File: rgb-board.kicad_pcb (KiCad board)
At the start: 2 copper layers, 178 x 129.5 mm, 91 parts, among them J1 Conn_02x25_Odd_Even, J10 RCJ-2223, J3 TEST_1P, J4 TEST_1P, J5 73415-3980, J6 73415-3980, J7 73415-3980, J8 73415-3980, J9 73415-3980, Q101 BC850C, Q105 BC850C, Q109 BC850C, Q113 BC850C, Q114 BC850C, Q201 BC850C, SW101 JS202011SCQN, SW105 JS202011SCQN, SW129 JS202011SCQN, SW143 JS202011SCQN, SW152 JS202011SCQN, U1 NCP1117-12_SOT223

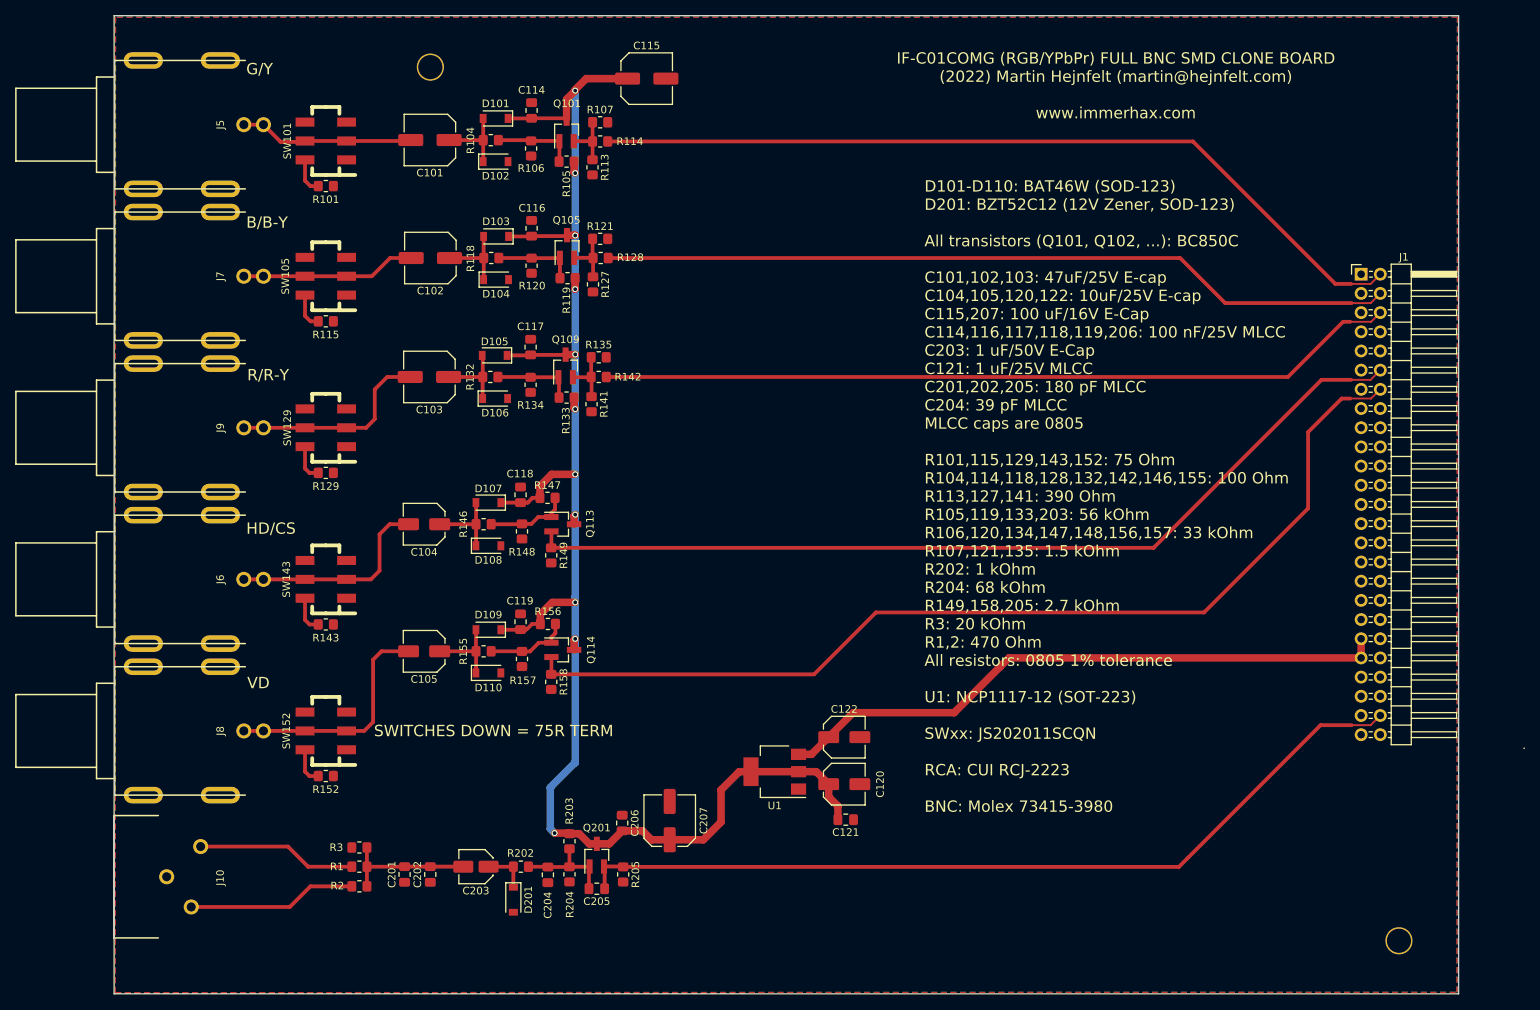
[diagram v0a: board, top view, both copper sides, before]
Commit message: Add optional segments, update to Kicad 6
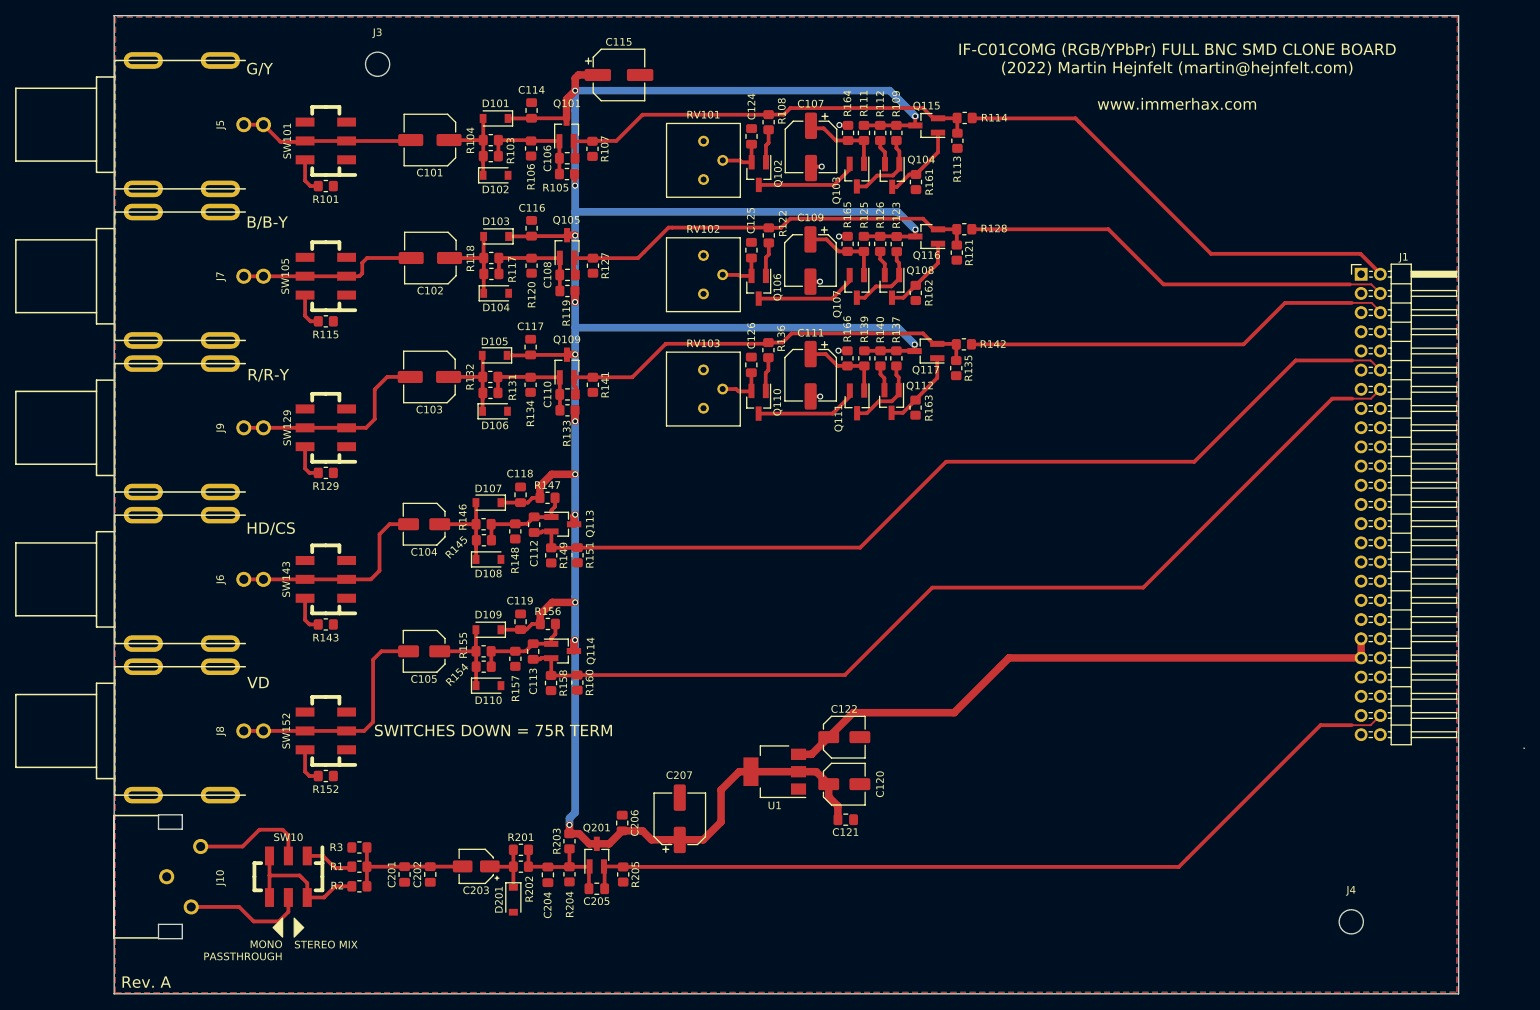
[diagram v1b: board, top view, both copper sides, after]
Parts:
- added C106: OPT, Capacitor_SMD:C_0805_2012Metric_Pad1.18x1.45mm_HandSolder, F.Cu at (109.8, 49.3)
- added C107: 100uF/16, Capacitor_SMD:CP_Elec_6.3x5.4, F.Cu at (142.1, 47.8)
- added C108: OPT, Capacitor_SMD:C_0805_2012Metric_Pad1.18x1.45mm_HandSolder, F.Cu at (109.9, 64.7)
- added C109: 100uF/16, Capacitor_SMD:CP_Elec_6.3x5.4, F.Cu at (142.0, 62.8)
- added C110: OPT, Capacitor_SMD:C_0805_2012Metric_Pad1.18x1.45mm_HandSolder, F.Cu at (109.9, 80.5)
- added C111: 100uF/16, Capacitor_SMD:CP_Elec_6.3x5.4, F.Cu at (142.0, 78.0)
- added C112: OPT, Capacitor_SMD:C_0805_2012Metric_Pad1.18x1.45mm_HandSolder, F.Cu at (105.4, 97.8)
- added C113: OPT, Capacitor_SMD:C_0805_2012Metric_Pad1.18x1.45mm_HandSolder, F.Cu at (105.3, 114.6)
- added C124: 15pF, Capacitor_SMD:C_0805_2012Metric_Pad1.18x1.45mm_HandSolder, F.Cu at (134.2, 46.4)
- added C125: 15pF, Capacitor_SMD:C_0805_2012Metric_Pad1.18x1.45mm_HandSolder, F.Cu at (134.2, 61.4)
- added C126: 15pF, Capacitor_SMD:C_0805_2012Metric_Pad1.18x1.45mm_HandSolder, F.Cu at (134.2, 76.6)
- added Q102: BC850C, Package_TO_SOT_SMD:SOT-23_Handsoldering, F.Cu at (135.2, 51.3)
- added Q103: BC850C, Package_TO_SOT_SMD:SOT-23_Handsoldering, F.Cu at (148.2, 51.5)
- added Q104: BC860C, Package_TO_SOT_SMD:SOT-23_Handsoldering, F.Cu at (152.8, 51.6)
- added Q106: BC850C, Package_TO_SOT_SMD:SOT-23_Handsoldering, F.Cu at (135.2, 66.4)
- added Q107: BC850C, Package_TO_SOT_SMD:SOT-23_Handsoldering, F.Cu at (148.2, 66.2)
- added Q108: BC860C, Package_TO_SOT_SMD:SOT-23_Handsoldering, F.Cu at (152.8, 66.2)
- added Q110: BC850C, Package_TO_SOT_SMD:SOT-23_Handsoldering, F.Cu at (135.2, 81.6)
- added Q111: BC850C, Package_TO_SOT_SMD:SOT-23_Handsoldering, F.Cu at (148.2, 81.5)
- added Q112: BC860C, Package_TO_SOT_SMD:SOT-23_Handsoldering, F.Cu at (152.8, 81.5)
- added Q115: OPT, Package_TO_SOT_SMD:SOT-23_Handsoldering, F.Cu at (157.4, 44.9)
- added Q116: OPT, Package_TO_SOT_SMD:SOT-23_Handsoldering, F.Cu at (157.4, 59.6)
- added Q117: OPT, Package_TO_SOT_SMD:SOT-23_Handsoldering, F.Cu at (157.3, 74.8)
- added R103: OPT, Resistor_SMD:R_0805_2012Metric_Pad1.20x1.40mm_HandSolder, F.Cu at (99.7, 49.0)
- added R108: OPT, Resistor_SMD:R_0805_2012Metric_Pad1.20x1.40mm_HandSolder, F.Cu at (136.5, 44.5)
- added R109: 470R, Resistor_SMD:R_0805_2012Metric_Pad1.20x1.40mm_HandSolder, F.Cu at (153.4, 45.9)
- added R111: 47k, Resistor_SMD:R_0805_2012Metric_Pad1.20x1.40mm_HandSolder, F.Cu at (149.1, 45.9)
- added R112: 470R, Resistor_SMD:R_0805_2012Metric_Pad1.20x1.40mm_HandSolder, F.Cu at (151.3, 45.9)
- added R117: 100, Resistor_SMD:R_0805_2012Metric_Pad1.20x1.40mm_HandSolder, F.Cu at (99.8, 64.6)
- added R122: OPT, Resistor_SMD:R_0805_2012Metric_Pad1.20x1.40mm_HandSolder, F.Cu at (136.5, 59.5)
- added R123: 470R, Resistor_SMD:R_0805_2012Metric_Pad1.20x1.40mm_HandSolder, F.Cu at (153.4, 60.6)
- added R125: 47k, Resistor_SMD:R_0805_2012Metric_Pad1.20x1.40mm_HandSolder, F.Cu at (149.1, 60.6)
- added R126: 470R, Resistor_SMD:R_0805_2012Metric_Pad1.20x1.40mm_HandSolder, F.Cu at (151.2, 60.6)
- added R131: OPT, Resistor_SMD:R_0805_2012Metric_Pad1.20x1.40mm_HandSolder, F.Cu at (99.6, 80.3)
- added R136: OPT, Resistor_SMD:R_0805_2012Metric_Pad1.20x1.40mm_HandSolder, F.Cu at (136.4, 74.7)
- added R137: 470R, Resistor_SMD:R_0805_2012Metric_Pad1.20x1.40mm_HandSolder, F.Cu at (153.4, 75.8)
- added R139: 47k, Resistor_SMD:R_0805_2012Metric_Pad1.20x1.40mm_HandSolder, F.Cu at (149.1, 75.8)
- added R140: 470R, Resistor_SMD:R_0805_2012Metric_Pad1.20x1.40mm_HandSolder, F.Cu at (151.3, 75.8)
- added R145: OPT, Resistor_SMD:R_0805_2012Metric_Pad1.20x1.40mm_HandSolder, F.Cu at (98.8, 99.8)
- added R151: OPT, Resistor_SMD:R_0805_2012Metric_Pad1.20x1.40mm_HandSolder, F.Cu at (111.2, 101.8)
- added R154: OPT, Resistor_SMD:R_0805_2012Metric_Pad1.20x1.40mm_HandSolder, F.Cu at (98.8, 116.6)
- added R160: OPT, Resistor_SMD:R_0805_2012Metric_Pad1.20x1.40mm_HandSolder, F.Cu at (111.2, 118.7)
- added R161: 470R, Resistor_SMD:R_0805_2012Metric_Pad1.20x1.40mm_HandSolder, F.Cu at (156.0, 52.4)
- added R162: 470R, Resistor_SMD:R_0805_2012Metric_Pad1.20x1.40mm_HandSolder, F.Cu at (156.0, 67.1)
- added R163: 470R, Resistor_SMD:R_0805_2012Metric_Pad1.20x1.40mm_HandSolder, F.Cu at (155.9, 82.3)
- added R164: 56k, Resistor_SMD:R_0805_2012Metric_Pad1.20x1.40mm_HandSolder, F.Cu at (147.0, 45.9)
- added R165: 56k, Resistor_SMD:R_0805_2012Metric_Pad1.20x1.40mm_HandSolder, F.Cu at (146.9, 60.6)
- added R166: 56k, Resistor_SMD:R_0805_2012Metric_Pad1.20x1.40mm_HandSolder, F.Cu at (146.9, 75.8)
- added R201: OPT, Resistor_SMD:R_0805_2012Metric_Pad1.20x1.40mm_HandSolder, F.Cu at (103.7, 140.8)
- added RV101: 500R, Potentiometer_THT:Potentiometer_Bourns_3386P_Vertical, F.Cu at (127.9, 52.1)
- added RV102: 500R, Potentiometer_THT:Potentiometer_Bourns_3386P_Vertical, F.Cu at (127.9, 67.2)
- added RV103: 500R, Potentiometer_THT:Potentiometer_Bourns_3386P_Vertical, F.Cu at (127.9, 82.4)
- added SW10: JS202011SCQN, JS202011SCQN:JS202011SCQN, F.Cu at (72.9, 144.4)
- C115, C207: value 100uF/16V -> 100uF/16; footprint Capacitor_SMD:C_Elec_6.3x5.4 -> Capacitor_SMD:CP_Elec_6.3x5.4
- C203: footprint Capacitor_SMD:C_Elec_4x5.4 -> Capacitor_SMD:CP_Elec_4x5.4
- D101, D102, D103, D104, D105, D106, D107, D108, D109, D110: value BAT46-TR -> BAT46W
- D201: value D_Zener -> BZT52C12
- J3, J4: value TEST_1P -> MountingHole; footprint Mounting_Holes:MountingHole_3.2mm_M3 -> MountingHole:MountingHole_3.2mm_M3
- R203: value 56K -> 56k
- R205: value 2.7K -> 2.7k
- moved R142 48.5 mm to (162.3, 73.9)
- moved R113 48.4 mm to (161.5, 47.0)
- moved R114 48.4 mm to (162.4, 43.9)
- moved R128 48.3 mm to (162.4, 58.7)
- moved R135 47.4 mm to (161.3, 77.1), turned to -90 degrees
- moved R121 47.3 mm to (161.4, 61.8), turned to -90 degrees
- moved J3 7.00 mm to (84.7, 36.8)
- moved J4 6.79 mm to (213.6, 150.4)
- moved C115 3.70 mm to (116.7, 38.3)
- moved R107 3.66 mm to (113.2, 48.0), turned to -90 degrees
- moved R141 2.57 mm to (113.2, 79.3)
- moved R127 2.48 mm to (113.2, 63.5)
- moved D104 1.82 mm to (100.4, 67.2)
- moved D102 1.82 mm to (100.3, 51.5)
- moved D108 1.80 mm to (99.4, 102.4)
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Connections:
- net /B/B-Y renamed /B/B-Y
- net /G/Y renamed /G/Y
- net /HD/CS renamed /HD/CS
- net /R/R-Y renamed /R/R-Y
- net Net-(Q101-Pad2) renamed G_Yp
- net Net-(Q105-Pad2) renamed B_BYp
- net Net-(Q109-Pad2) renamed R_RYp
- J1 pad 10: (no net) -> unconnected-(J1-Pad10)
- J1 pad 15: (no net) -> unconnected-(J1-Pad15)
- J1 pad 16: (no net) -> unconnected-(J1-Pad16)
- J1 pad 17: (no net) -> unconnected-(J1-Pad17)
- J1 pad 18: (no net) -> unconnected-(J1-Pad18)
- J1 pad 20: (no net) -> unconnected-(J1-Pad20)
- J1 pad 22: (no net) -> unconnected-(J1-Pad22)
- J1 pad 23: (no net) -> unconnected-(J1-Pad23)
- J1 pad 24: (no net) -> unconnected-(J1-Pad24)
- J1 pad 26: (no net) -> unconnected-(J1-Pad26)
- J1 pad 27: (no net) -> unconnected-(J1-Pad27)
- J1 pad 28: (no net) -> unconnected-(J1-Pad28)
- J1 pad 29: (no net) -> unconnected-(J1-Pad29)
- J1 pad 30: (no net) -> unconnected-(J1-Pad30)
- J1 pad 32: (no net) -> unconnected-(J1-Pad32)
- J1 pad 33: (no net) -> unconnected-(J1-Pad33)
- J1 pad 34: (no net) -> unconnected-(J1-Pad34)
- J1 pad 35: (no net) -> unconnected-(J1-Pad35)
- J1 pad 36: (no net) -> unconnected-(J1-Pad36)
- J1 pad 37: (no net) -> unconnected-(J1-Pad37)
- J1 pad 38: (no net) -> unconnected-(J1-Pad38)
- J1 pad 40: (no net) -> unconnected-(J1-Pad40)
- J1 pad 42: (no net) -> unconnected-(J1-Pad42)
- J1 pad 43: (no net) -> unconnected-(J1-Pad43)
- J1 pad 44: (no net) -> unconnected-(J1-Pad44)
- J1 pad 45: (no net) -> unconnected-(J1-Pad45)
- J1 pad 46: (no net) -> unconnected-(J1-Pad46)
- J1 pad 8: (no net) -> unconnected-(J1-Pad8)
- J1 pad 9: (no net) -> unconnected-(J1-Pad9)
- R1 pad 2: /AUDIO_R -> /AUDIO_R_SW
- R2 pad 1: /AUDIO_L -> /AUDIO_L_SW
- SW101 pad 1: (no net) -> unconnected-(SW101-Pad1)
- SW101 pad 3: (no net) -> unconnected-(SW101-Pad3)
- SW101 pad 6: (no net) -> unconnected-(SW101-Pad6)
- SW105 pad 1: (no net) -> unconnected-(SW105-Pad1)
- SW105 pad 3: (no net) -> unconnected-(SW105-Pad3)
- SW105 pad 6: (no net) -> unconnected-(SW105-Pad6)
- SW129 pad 1: (no net) -> unconnected-(SW129-Pad1)
- SW129 pad 3: (no net) -> unconnected-(SW129-Pad3)
- SW129 pad 6: (no net) -> unconnected-(SW129-Pad6)
- SW143 pad 1: (no net) -> unconnected-(SW143-Pad1)
- SW143 pad 3: (no net) -> unconnected-(SW143-Pad3)
- SW143 pad 6: (no net) -> unconnected-(SW143-Pad6)
- SW152 pad 1: (no net) -> unconnected-(SW152-Pad1)
- SW152 pad 3: (no net) -> unconnected-(SW152-Pad3)
- SW152 pad 6: (no net) -> unconnected-(SW152-Pad6)
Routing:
- net +12V: track 219.6 -> 374.5 mm, vias 11 -> 14
- net R_RYp: track 7.67 -> 58.3 mm
- net B_BYp: track 7.57 -> 57.2 mm
- net G_Yp: track 7.48 -> 57.0 mm
- net /R-Y: track 106.0 -> 57.0 mm
- net /Y: track 110.6 -> 62.6 mm
- net /B-Y: track 105.2 -> 57.6 mm
- net /AUDIO_L_SW: track 0.00 -> 20.0 mm
- net Net-(Q106-Pad3): track 0.00 -> 13.8 mm
- net Net-(Q110-Pad3): track 0.00 -> 13.8 mm
- net Net-(Q102-Pad3): track 0.00 -> 13.6 mm
- net Net-(C111-Pad1): track 0.00 -> 11.0 mm
- net Net-(C109-Pad1): track 0.00 -> 10.9 mm
- net Net-(Q112-Pad3): track 0.00 -> 10.6 mm
- net Net-(C107-Pad1): track 0.00 -> 10.6 mm
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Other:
- outline, holes or cut-outs redrawn
- net class Default removed
- board text added: "MONO PASSTHROUGH"
- board text added: "Rev. A"
- board text added: "STEREO MIX"
- board text removed: "D101-D110: BAT46W (SOD-123) D201: BZT52C12 (12V Zener, SOD-123) All transistors (Q101, Q102, ...): BC850C C101,102,103: 47uF/25V E-cap C104,105,120,122: 10uF/25V E-cap C115,207: 100 uF/16V E-Cap C114,116,117,118,119,206: 100 nF/25V MLCC C203: 1 uF/50V E-Cap C121: 1 uF/25V MLCC C201,202,205: 180 pF MLCC C204: 39 pF MLCC MLCC caps are 0805 R101,115,129,143,152: 75 Ohm R104,114,118,128,132,142,146,1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"

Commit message: Update PCB, and plots
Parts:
- moved R107 48.3 mm to (161.5, 47.0)
- moved R113 48.3 mm to (113.2, 48.0)
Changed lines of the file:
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@@
   )
   (footprint "Resistor_SMD:R_0805_2012Metric_Pad1.20x1.40mm_HandSolder" (layer "F.Cu")
-    (at 113.157 48.0314 -90)
+    (at 161.4678 46.9646 -90)
     (descr "Resistor SMD 0805 (2012 Metric), square (rectangular) end terminal, IPC_7351 nominal with elongated pad for handsoldering. (Body size source: IPC-SM-782 page 72, https://www.pcb-3d.com/wordpress/wp-content/uploads/ipc-sm-782a_amendment_1_and_2.pdf), generated with kicad-footprint-generator")
     (tags "resistor handsolder")
@@
   )
   (footprint "Resistor_SMD:R_0805_2012Metric_Pad1.20x1.40mm_HandSolder" (layer "F.Cu")
-    (at 161.4678 46.9646 -90)
-    (descr "Resistor SMD 0805 (2012 Metric), square (rectangular) end terminal, IPC_7351 nominal with elongated pad for handsoldering. (Body size source: IPC-SM-782 page 72, https://www.pcb-3d.com/wordpress/wp-content/uploads/ipc-sm-782a_amendment_1_and_2.pdf), generated with kicad-footprint-generator")
-    (tags "resistor handsolder")
+    (at 113.157 48.0314 -90)
+    (descr "Resistor SMD 0805 (2012 Metric), square (rectangular) end terminal, IPC_7351 nominal with elongated pad for handsoldering. (Body size source: IPC-SM-782 page 72, https://www.pcb-3d.com/wordpress/wp-content/uploads/ipc-sm-782a_amendment_1_and_2.pdf), generated with kicad-footprint-generator")
+    (tags "resistor handsolder")
